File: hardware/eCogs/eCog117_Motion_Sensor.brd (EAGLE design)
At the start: 47.5 x 28 mm, 4 parts

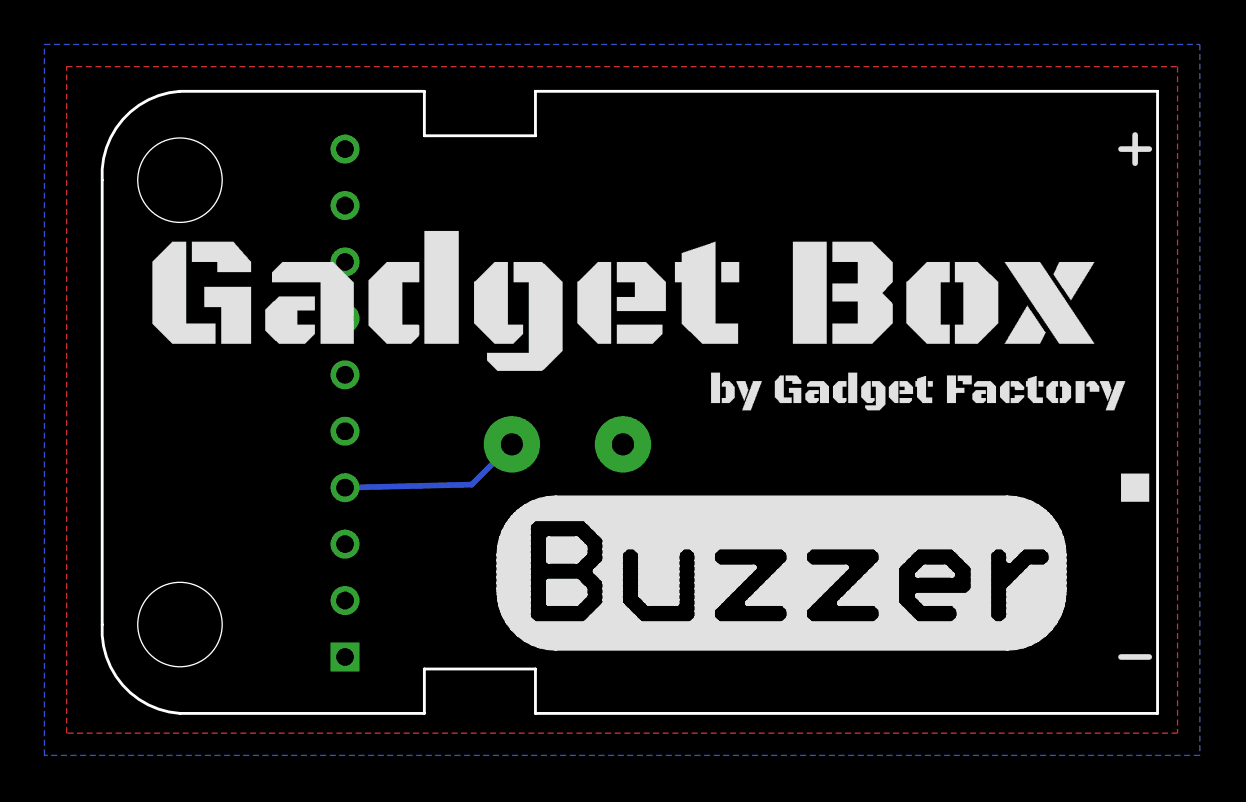
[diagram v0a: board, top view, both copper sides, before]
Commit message: Update eCogs to through hole
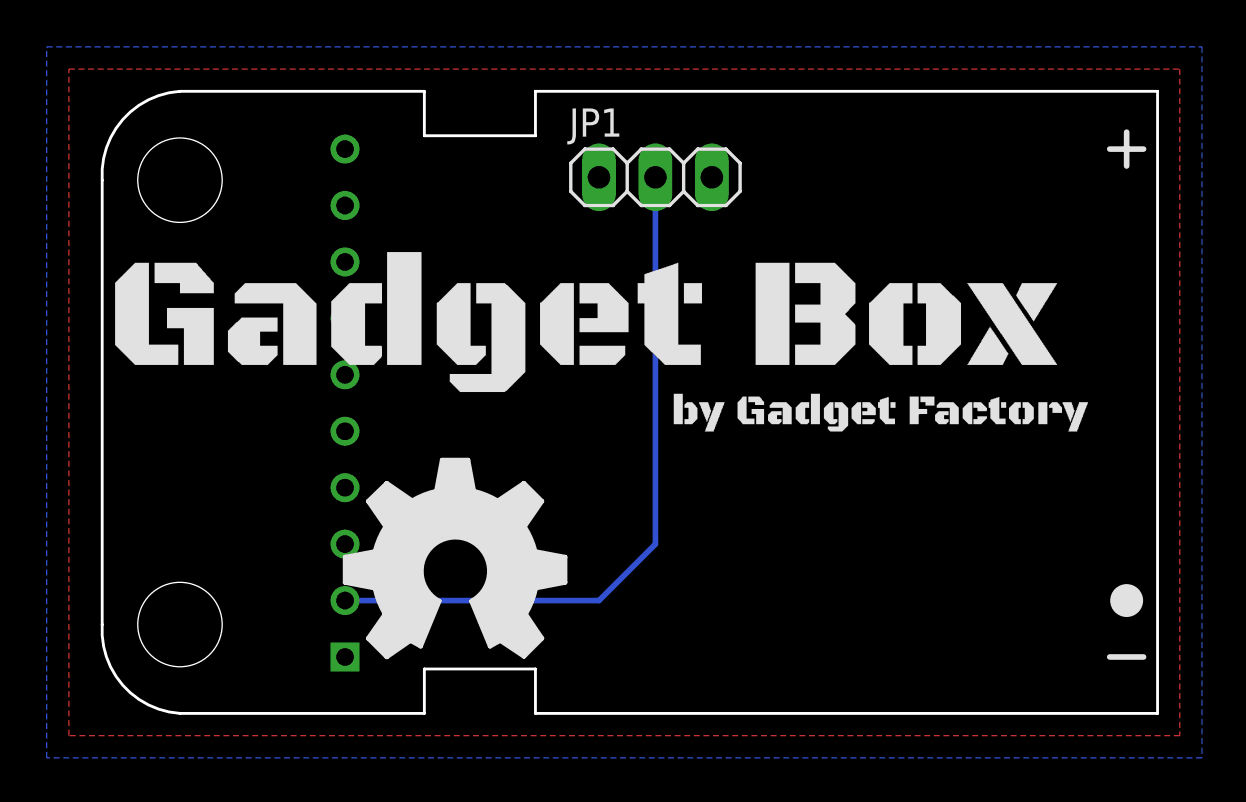
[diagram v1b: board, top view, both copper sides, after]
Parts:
- removed SP1: SPEAKER/PS12, adafruit:PS12
- removed U$4: (no value), eCogs:LEGEND_PWM
- added JP1: (no value), pinhead:1X03
- added U$10: (no value), ohw-logo:OSHW_FILLX350_NOTEXT
- added U$2: (no value), eCogs:LEGEND_DIO
- moved U$1 1.93 mm to (22.4, 17.4)
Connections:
- net 3V3: now also JP1.1
- net GND: now also JP1.3; no longer SP1.P$1
- net N$1: now also ECOG.G0, JP1.2; no longer ECOG.G2, SP1.P$2
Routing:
- net N$1: track 8.26 -> 31.5 mm
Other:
- board text added: "Motion Sensor"
- board text added: "XC0 Motion"
- board text added: "ecog117 v2.0"
- board text added: "ecog117.GadgetFactory.net"
- board text removed: "2"
- board text removed: "Buzzer"
- board text removed: "ecog110 v2.1"
- board text removed: "ecog110.GadgetFactory.net"
